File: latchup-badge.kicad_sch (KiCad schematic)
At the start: 42 parts, among them J1 USB_B_Micro, J2 Connector_Generic:Conn_02x06_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, J3 Connector_Generic:Conn_02x06_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, J4 Connector_Generic:Conn_02x05_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, SW1 SW_Push, SW2 SW_Push, U1 ICE40UP5K-SG48ITR, U2 TLV70012_SOT23-5, U3 TLV70033_SOT23-5, U4 M25PX32-VMW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

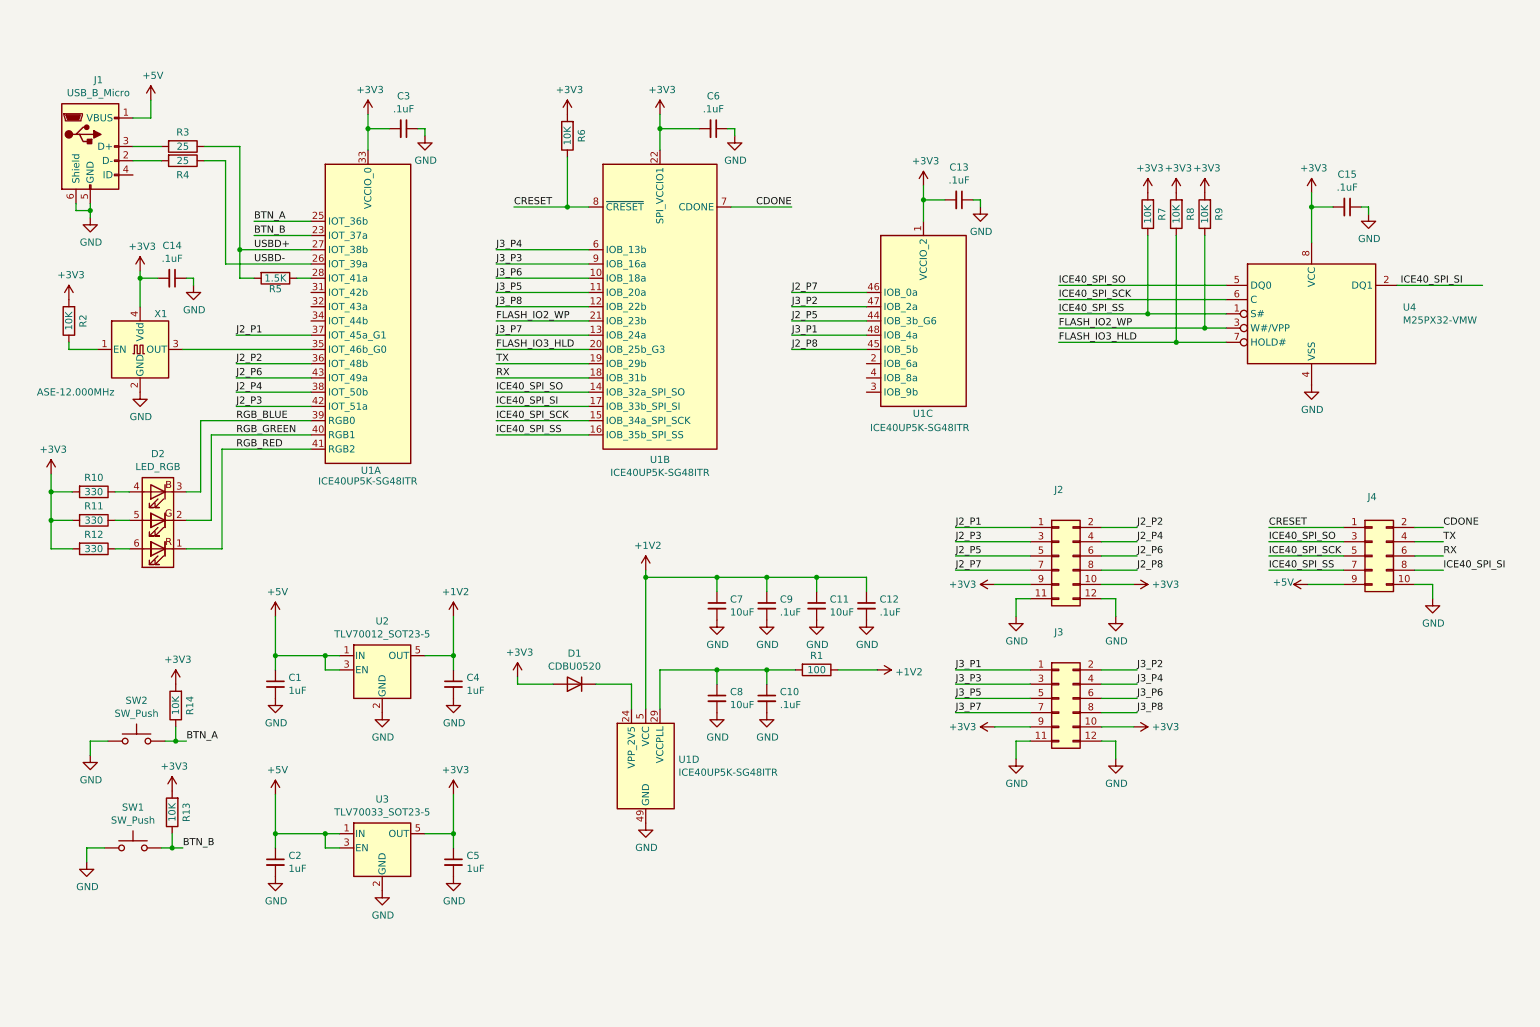
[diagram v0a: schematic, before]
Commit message: Switch to USB-C connector and shrink board
Signed-off-by: Michael Welling <mwelling@ieee.org>
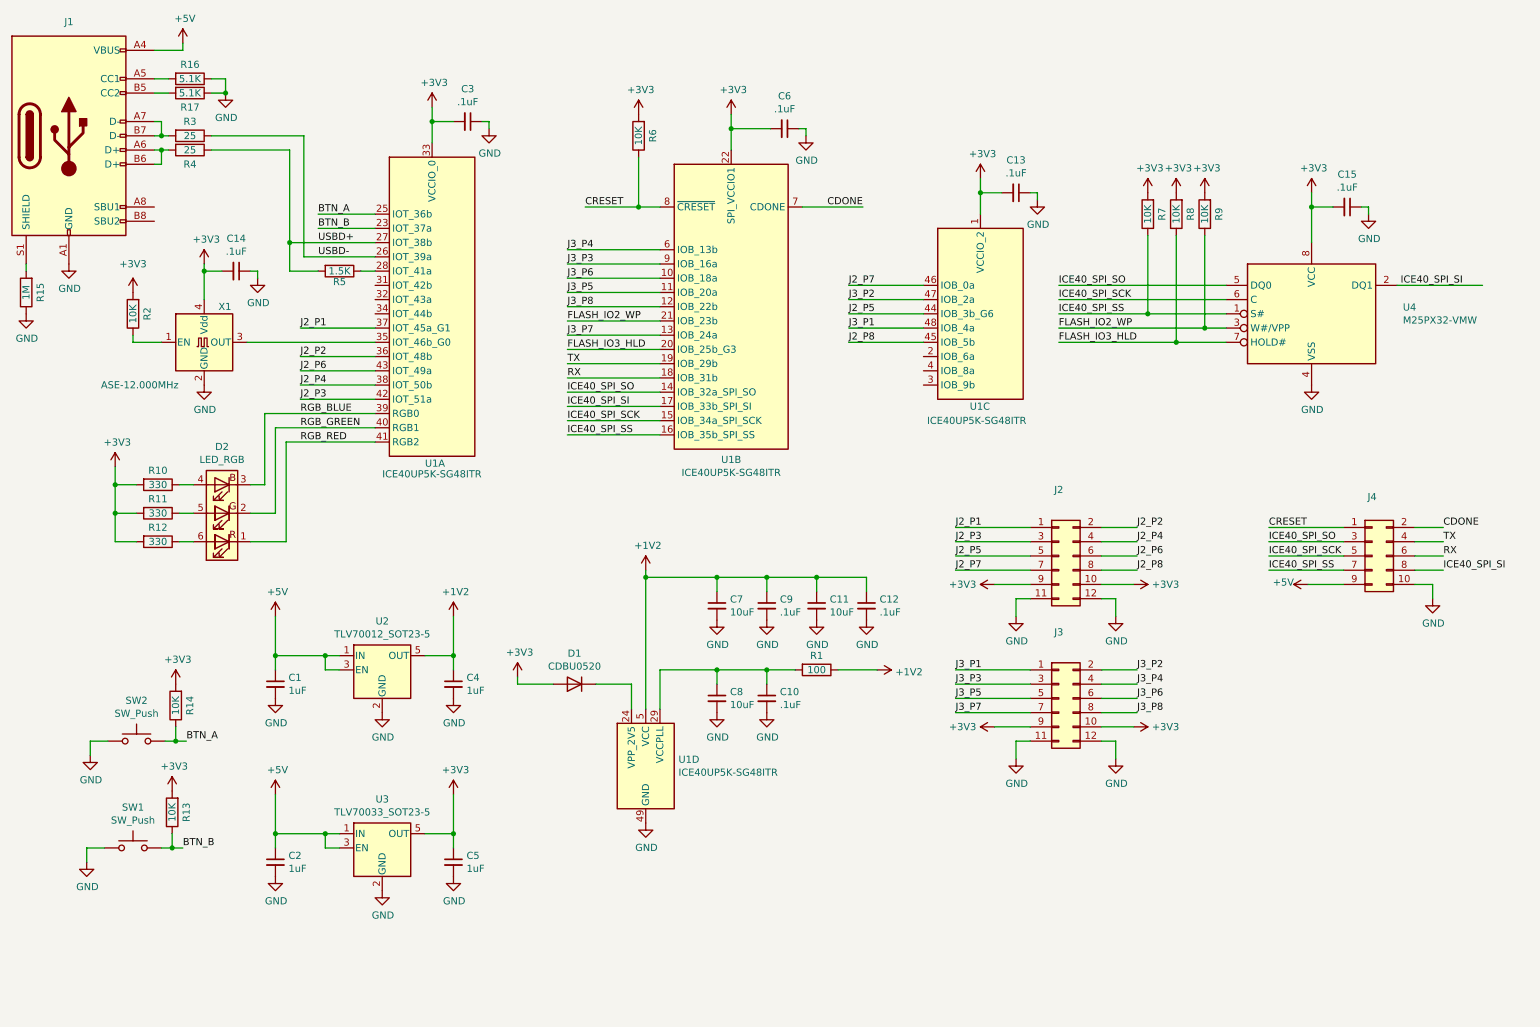
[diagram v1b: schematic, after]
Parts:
- removed J1: USB_B_Micro, Connector_USB:USB_Micro-B_Molex-105017-0001, symbol Connector:USB_B_Micro
- added J1: USB_C_Receptacle_USB2.0, Connector_USB:USB_C_Receptacle_HRO_TYPE-C-31-M-12, symbol Connector:USB_C_Receptacle_USB2.0
- added R15: 1M, Resistor_SMD:R_0402_1005Metric, symbol Device:R
- added R16, R17: 5.1K, Resistor_SMD:R_0402_1005Metric, symbol Device:R
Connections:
- net +5V: now also J1.A4 (VBUS), J1.A9 (VBUS), J1.B4 (VBUS), J1.B9 (VBUS)
- net GND: now also J1.A1 (GND), J1.A12 (GND), J1.B1 (GND), J1.B12 (GND), R15.1, R16.1, R17.1
- net USBD+: now also R4.1; no longer R3.1
- net USBD-: now also R3.1; no longer R4.1
- net at R4.2: now also J1.A6 (D+), J1.B6 (D+)
- net at R3.2: now also J1.A7 (D-), J1.B7 (D-)
- new net: J1.A5 (CC1), R16.2
- new net: J1.B5 (CC2), R17.2
- new net: J1.S1 (SHIELD), R15.2
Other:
- moved on the sheet: C13, C14, C3, C6, D2, R10, R11, R12, R2, R3, R4, R5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

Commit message: Add PSRAM
Signed-off-by: Michael Welling <mwelling@ieee.org>
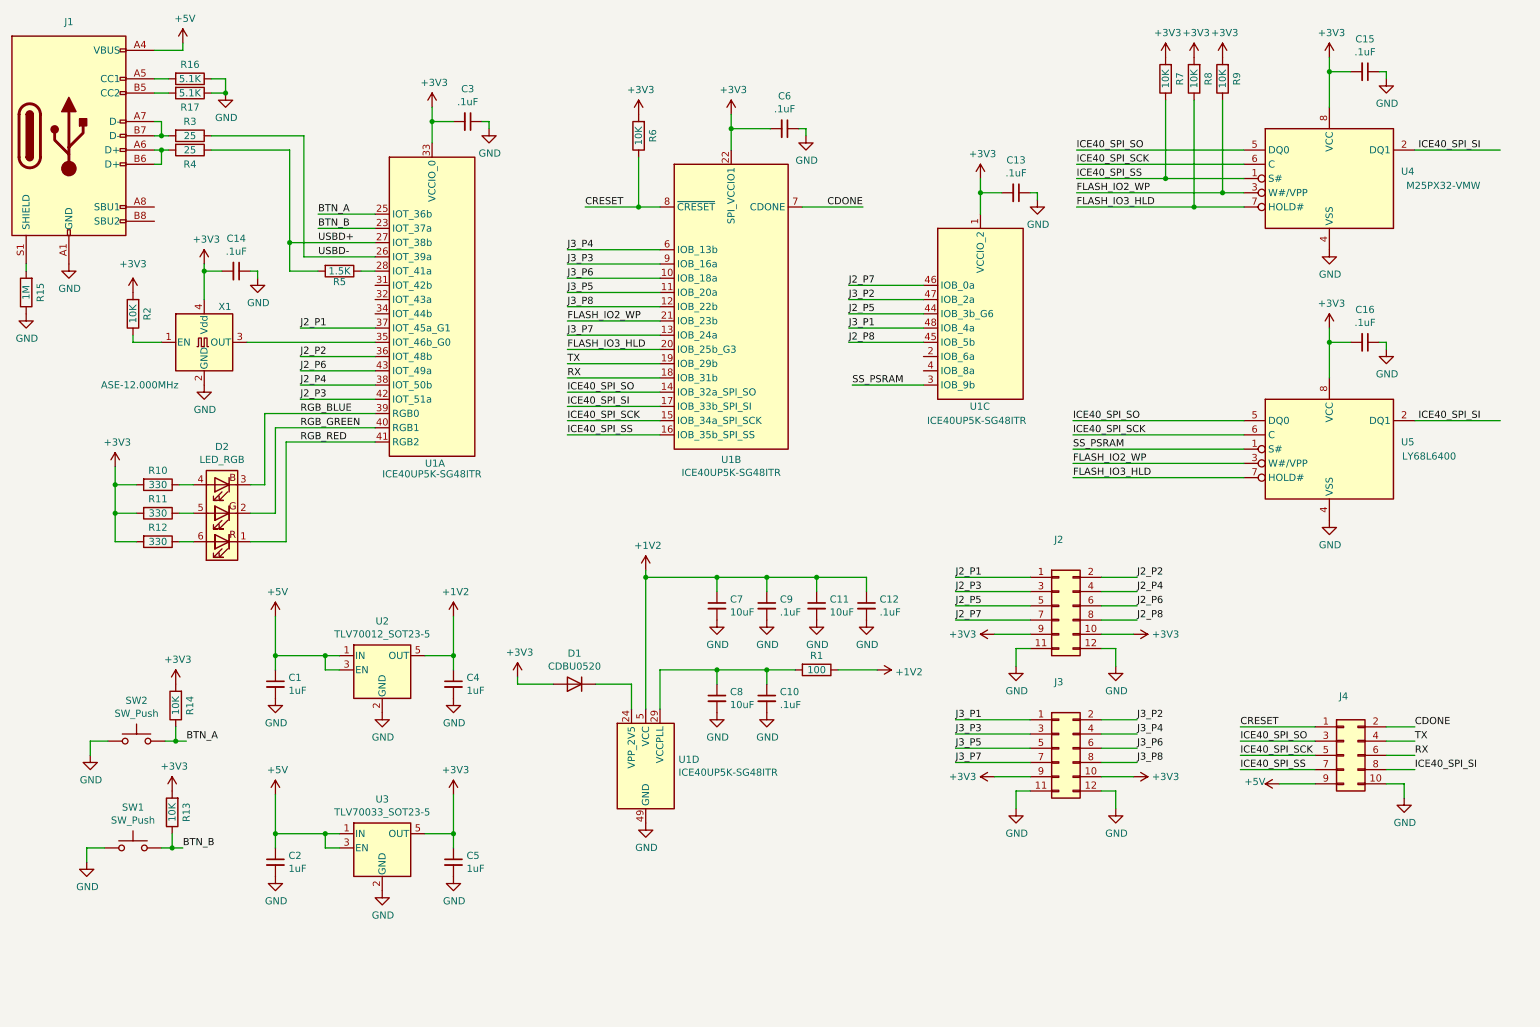
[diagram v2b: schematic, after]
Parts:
- added C16: .1uF, Capacitor_SMD:C_0402_1005Metric, symbol Device:C_Small
- added U5: LY68L6400, Package_SO:SOIC-8W_5.3x5.3mm_P1.27mm, symbol Memory_Flash:M25PX32-VMW
- U4: footprint Package_SO:SOIJ-8_5.3x5.3mm_P1.27mm -> Package_SO:SOIC-8W_5.3x5.3mm_P1.27mm
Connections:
- net +3V3: now also C16.2, U5.8 (VCC)
- net FLASH_IO2_WP: now also U5.3 (W#/VPP)
- net FLASH_IO3_HLD: now also U5.7 (HOLD#)
- net GND: now also C16.1, U5.4 (VSS)
- net ICE40_SPI_SCK: now also U5.6 (C)
- net ICE40_SPI_SI: now also U5.2 (DQ1)
- net ICE40_SPI_SO: now also U5.5 (DQ0)
- net SS_PSRAM: now reaches U1.3 (IOB_9b)
- net SS_PSRAM: now also U5.1 (S#)
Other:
- moved on the sheet: C15, J2, J3, J4, R7, R8, R9

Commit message: Update PSRAM footprint
Signed-off-by: Michael Welling <mwelling@ieee.org>
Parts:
- U5: footprint Package_SO:SOIC-8W_5.3x5.3mm_P1.27mm -> Package_SO:SOIC-8_3.9x4.9mm_P1.27mm
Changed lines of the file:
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@@
     (property "Reference" "U5" (id 0) (at 264.16 92.71 0))
     (property "Value" "LY68L6400" (id 1) (at 267.97 95.25 0))
-    (property "Footprint" "Package_SO:SOIC-8W_5.3x5.3mm_P1.27mm" (id 2) (at 266.7 92.71 0)
+    (property "Footprint" "Package_SO:SOIC-8_3.9x4.9mm_P1.27mm" (id 2) (at 266.7 92.71 0)
       (effects (font (size 1.27 1.27)) hide)
     )
@@
     )
     (path "/3247ef77-07f5-4edb-8ad9-281bf3ceaa42"
-      (reference "U5") (unit 1) (value "LY68L6400") (footprint "Package_SO:SOIC-8W_5.3x5.3mm_P1.27mm")
+      (reference "U5") (unit 1) (value "LY68L6400") (footprint "Package_SO:SOIC-8_3.9x4.9mm_P1.27mm")
     )
     (path "/00000000-0000-0000-0000-00005c9d2b97"

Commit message: Use the PMOD pinout from icebreaker bitsy breakout
Signed-off-by: Michael Welling <mwelling@ieee.org>
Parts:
- removed R13: 10K, Resistor_SMD:R_0402_1005Metric, symbol Device:R
- added J5: Connector_Generic:Conn_02x06_Odd_Even, Connector_PinSocket_2.54mm:PinSocket_2x06_P2.54mm_Horizontal, symbol Connector_Generic:Conn_02x06_Odd_Even
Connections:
- net +3V3: now also J2.1 (Pin_1), J2.2 (Pin_2), J3.1 (Pin_1), J3.2 (Pin_2), J5.1 (Pin_1), J5.2 (Pin_2); no longer J2.10 (Pin_10), J2.9 (Pin_9), J3.10 (Pin_10), J3.9 (Pin_9)
- net BTN_A: now also U1.2 (IOB_6a); no longer U1.25 (IOT_36b)
- net CRESET: now also SW1.2
- net FLASH_IO2_WP: now also U1.18 (IOB_31b); no longer U1.21 (IOB_23b)
- net FLASH_IO3_HLD: now also U1.19 (IOB_29b); no longer U1.20 (IOB_25b_G3)
- net GND: now also J2.3 (Pin_3), J2.4 (Pin_4), J3.3 (Pin_3), J3.4 (Pin_4), J5.3 (Pin_3), J5.4 (Pin_4); no longer J2.11 (Pin_11), J2.12 (Pin_12), J3.11 (Pin_11), J3.12 (Pin_12)
- net SS_PSRAM: now also U1.6 (IOB_13b); no longer U1.3 (IOB_9b)
- net PIN28: now reaches U1.28 (IOT_41a)
- net PIN28: now also J3.5 (Pin_5); no longer R5.1
- net PIN31: now reaches U1.31 (IOT_42b)
- net PIN31: now also J3.10 (Pin_10)
- net PIN32: now reaches U1.32 (IOT_43a)
- net PIN32: now also J3.9 (Pin_9)
- net PIN34: now reaches U1.34 (IOT_44b)
- net PIN34: now also J3.6 (Pin_6)
- net PIN35: now reaches U1.35 (IOT_46b_G0), X1.3 (OUT)
- net PIN4: now reaches U1.4 (IOB_8a)
- net PIN4: now also J2.7 (Pin_7)
- net BTN_B renamed PIN23
- net PIN23: now also J5.11 (Pin_11); no longer SW1.2
- net J2_P1 renamed USB_DET
- net USB_DET: now also R5.1; no longer J2.1 (Pin_1)
- net J2_P2 renamed PIN36
- net PIN36: now also J3.12 (Pin_12); no longer J2.2 (Pin_2)
- net J2_P3 renamed USBD_P
- net USBD_P: now also R4.1, R5.2; no longer J2.3 (Pin_3)
- net J2_P4 renamed USBD_N
- net USBD_N: now also R3.1; no longer J2.4 (Pin_4)
- net J2_P5 renamed PIN44
- net PIN44: now also J2.12 (Pin_12); no longer J2.5 (Pin_5)
- net J2_P6 renamed PIN10
- net PIN10: now also U1.10 (IOB_18a); no longer U1.43 (IOT_49a)
- net J2_P7 renamed PIN46
- net PIN46: now also J5.6 (Pin_6); no longer J2.7 (Pin_7)
- net J2_P8 renamed PIN3
- net PIN3: now also U1.3 (IOB_9b); no longer U1.45 (IOB_5b)
- net J3_P1 renamed PIN48
- net PIN48: now also J2.9 (Pin_9); no longer J3.1 (Pin_1)
- net J3_P2 renamed PIN47
- net PIN47: now also J2.11 (Pin_11); no longer J3.2 (Pin_2)
- net J3_P3 renamed PIN9
- net PIN9: now also J2.5 (Pin_5); no longer J3.3 (Pin_3)
- removed net J3_P4: J3.4 (Pin_4), U1.6 (IOB_13b)
- net J3_P5 renamed PIN11
- net PIN11: now also J5.5 (Pin_5); no longer J3.5 (Pin_5)
- removed net J3_P6: J3.6 (Pin_6), U1.10 (IOB_18a)
- net J3_P7 renamed PIN13
- net PIN13: now also J5.7 (Pin_7); no longer J3.7 (Pin_7)
- net J3_P8 renamed PIN12
- net PIN12: now also J5.9 (Pin_9); no longer J3.8 (Pin_8)
- net RX: no longer names the net of J4.6 (Pin_6)
- net RX: no longer U1.18 (IOB_31b)
- net TX: no longer names the net of J4.4 (Pin_4)
- net TX: no longer U1.19 (IOB_29b)
- removed net USBD+: R4.1, R5.2, U1.27 (IOT_38b)
- net USBD- renamed PIN26
- net PIN26: now also J3.7 (Pin_7); no longer R3.1
- new net PIN20: J5.8 (Pin_8), U1.20 (IOB_25b_G3)
- new net PIN21: J5.10 (Pin_10), U1.21 (IOB_23b)
- new net PIN25: J5.12 (Pin_12), U1.25 (IOT_36b)
- new net PIN27: J3.8 (Pin_8), U1.27 (IOT_38b)
- new net PIN43: J3.11 (Pin_11), U1.43 (IOT_49a)
- new net PIN45: J2.10 (Pin_10), U1.45 (IOB_5b)
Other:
- moved on the sheet: J2, J3, J4, R5

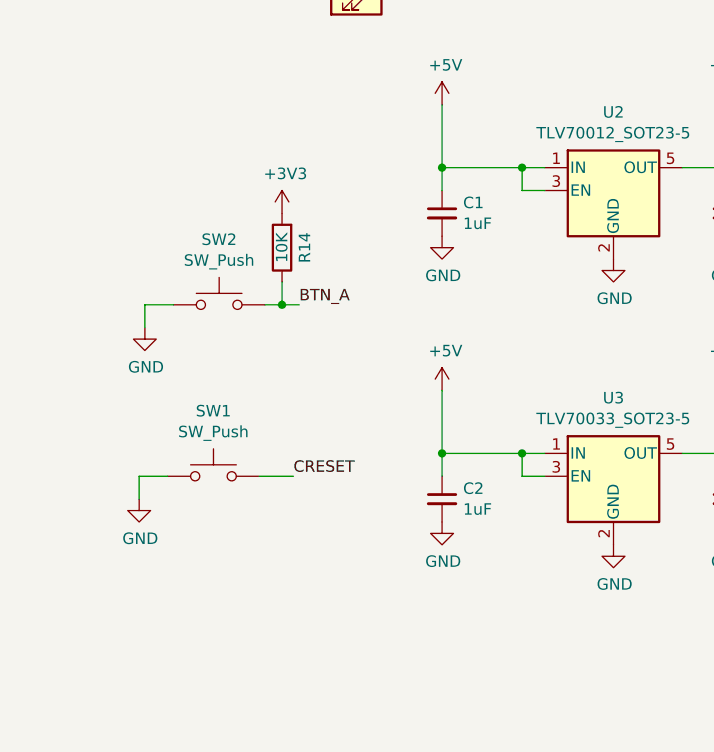
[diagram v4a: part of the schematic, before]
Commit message: Add delay to 3.3V enable
The 1.2V rail should be up before 3.3V.

Signed-off-by: Michael Welling <mwelling@ieee.org>
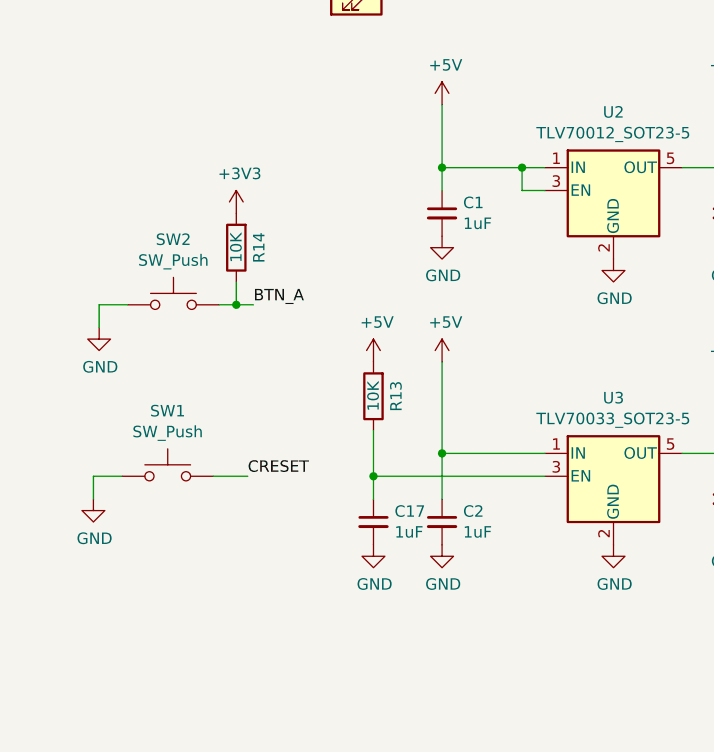
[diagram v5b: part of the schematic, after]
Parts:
- added C17: 1uF, Capacitor_SMD:C_0603_1608Metric, symbol Device:C_Small
- added R13: 10K, Resistor_SMD:R_0402_1005Metric, symbol Device:R
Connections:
- net +5V: now also R13.2; no longer U3.3 (EN)
- net GND: now also C17.2
- new net: C17.1, R13.1, U3.3 (EN)
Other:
- moved on the sheet: C2, R14, SW1, SW2
